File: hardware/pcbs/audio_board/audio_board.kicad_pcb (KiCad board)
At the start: 4 copper layers, 152 x 117.3 mm, 150 parts, among them J1 I2C, J10 Stereo Line-in, J2 Conn_01x08, J3 NC3MAH, J4 AudioJack3, J5 NC3MAH, J6 NC3FAH1, J7 NC3FAH1, J8 NC3FAH1, J9 DECT, Q1 S8050, Q2 2N7002, Q3 SI2309CDS-T1-GE3, Q4 2N7002, Q5 SI2309CDS-T1-GE3, Q6 2N7002, Q7 SI2309CDS-T1-GE3, U2 LP5907MFX-3.3, U3 LM5158, U4 TAD5242, U5 TAD5242, U6 TAA3040

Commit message: route some more
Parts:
- added C9: 0.1uF, Capacitor_SMD:C_0805_2012Metric, F.Cu at (88.5, 99.8)
- added R54: 510, Resistor_SMD:R_0805_2012Metric, F.Cu at (191.0, 92.5)
- C4: value 22uF -> 47uF; footprint Capacitor_SMD:C_0805_2012Metric -> Capacitor_THT:CP_Radial_D5.0mm_P2.00mm
- moved J1 129.0 mm to (89.5, 91.5)
- moved C1 120.8 mm to (85.0, 126.1), turned to 180 degrees
- moved D2 119.6 mm to (85.8, 118.8), turned to 180 degrees
- moved L1 119.4 mm to (73.2, 118.8), turned to 0 degrees
- moved Q1 119.2 mm to (75.8, 122.0)
- moved U2 119.0 mm to (86.0, 122.4), turned to 90 degrees
- moved R10 118.8 mm to (72.8, 122.0)
- moved C3 118.8 mm to (89.0, 122.0)
- moved C33 118.5 mm to (173.8, 111.8)
- moved C34 117.3 mm to (173.8, 108.0)
- moved C29 117.0 mm to (161.8, 107.0), turned to 135 degrees
- moved R6 116.1 mm to (127.5, 94.5)
- moved D1 116.1 mm to (80.2, 125.8)
- moved C28 115.8 mm to (163.5, 110.8), turned to 135 degrees
- moved C4 115.6 mm to (80.8, 122.0)
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- renumbered C9 to C10, C10 to C11, C11 to C12, C12 to C13, C13 to C14, C14 to C15, C15 to C16, C16 to C17, C17 to C18, C18 to C19, C19 to C20, C20 to C21, C21 to C22, C22 to C23, C23 to C24, C24 to C25, C25 to C26, C26 to C27, C27 to C28, C28 to C29, C29 to C30, C30 to C31, C31 to C32, C32 to C33, C33 to C34, C34 to C35, C35 to C36, C36 to C37, C37 to C38, C38 to C39, C39 to C40, C40 to C41, C41 to C42, C42 to C43, C43 to C44, C44 to C45, C45 to C46, C46 to C47, C47 to C48, C48 to C49, C49 to C50, C50 to C51, C51 to C52, C52 to C53, C53 to C54, R54 to R55, R55 to R56
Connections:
- C41 pad 2: /ADC/IN1+ -> /ADC/IN2+
- C42 pad 2: /ADC/IN1- -> /ADC/IN2-
- C47 pad 2: /ADC/IN2+ -> /ADC/IN1+
- C48 pad 2: /ADC/IN2- -> /ADC/IN1-
- D4 pad 2: /ADC/IN1+ -> /ADC/IN2+
- D4 pad 3: /ADC/IN1- -> /ADC/IN2-
- D5 pad 2: /ADC/IN2+ -> /ADC/IN1+
- D5 pad 3: /ADC/IN2- -> /ADC/IN1-
- J10 pad S: GND -> /ADC/IN4-
- Q2 pad 1: /PHANTOM_IN1_EN -> /PHANTOM_IN2_EN
- Q4 pad 1: /PHANTOM_IN2_EN -> /PHANTOM_IN1_EN
- R18 pad 1: /PHANTOM_IN1_EN -> /PHANTOM_IN2_EN
- R28 pad 1: /ADC/IN1+ -> /ADC/IN2+
- R29 pad 2: /ADC/IN1- -> /ADC/IN2-
- R30 pad 1: /PHANTOM_IN2_EN -> /PHANTOM_IN1_EN
- R40 pad 1: /ADC/IN2+ -> /ADC/IN1+
- R41 pad 2: /ADC/IN2- -> /ADC/IN1-
- U6 pad 13: GND -> /ADC/IN4-
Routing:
- net +48V: track 8.09 -> 212.0 mm
- net +3.3VA: track 22.6 -> 197.3 mm, vias 3 -> 8
- net GND: track 18.0 -> 135.4 mm, vias 24 -> 32
- net /ADC/IN1+: track 8.14 -> 46.8 mm
- net /ADC/IN1-: track 8.08 -> 44.5 mm
- net /ADC/IN4-: track 0.00 -> 36.3 mm
- net +5V: track 36.7 -> 67.9 mm
- net /ADC/IN3-: track 8.08 -> 33.9 mm
- net /ADC/IN3+: track 8.14 -> 30.1 mm
- net +5VA: track 0.00 -> 19.3 mm
- net Net-(J10-PadT): track 0.00 -> 14.0 mm
- net /ADC/IN4+: track 0.00 -> 13.7 mm
- net +3.3V: track 19.1 -> 32.2 mm, vias 0 -> 2
- net Net-(J10-PadR): track 0.00 -> 11.5 mm
- net Net-(D1-K): track 0.00 -> 11.0 mm
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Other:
- board size 152 x 117.3 mm -> 152 x 61.5 mm

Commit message: routing almost complete
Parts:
- added C5: 1μF, Capacitor_SMD:C_0805_2012Metric, F.Cu at (175.0, 123.0)
- added C6: 1μF, Capacitor_SMD:C_0805_2012Metric, F.Cu at (119.0, 128.0)
- J9: value DECT -> Conn_01x12; footprint extra:DectModule -> Connector_PinHeader_2.54mm:PinHeader_1x12_P2.54mm_Vertical
- moved J9 94.9 mm to (99.5, 109.5), turned to 90 degrees
- moved J1 31.2 mm to (109.4, 115.5), turned to 90 degrees
- moved J10 22.8 mm to (206.8, 98.2)
- moved R54 11.5 mm to (200.2, 99.2), turned to 90 degrees
- moved J2 1.38 mm to (178.6, 97.8)
- moved R6 0.75 mm to (127.5, 93.8), turned to -90 degrees
- moved Q4 0.75 mm to (127.1, 135.4)
- moved R32 0.40 mm to (128.7, 132.5)
- moved R30 0.29 mm to (124.2, 135.2)
- moved U1 0.16 mm to (102.0, 98.2)
- turned R1 to -90 degrees
- turned R2 to -90 degrees
- turned R3 to -90 degrees
- turned R4 to -90 degrees
- renumbered C8 to C10, C9 to C11, C10 to C12, C11 to C13, C12 to C14, C13 to C15, C14 to C16, C15 to C17, C16 to C18, C17 to C19, C18 to C20, C19 to C21, C20 to C22, C21 to C23, C22 to C24, C23 to C25, C24 to C26, C25 to C27, C26 to C28, C27 to C29, C28 to C30, C29 to C31, C30 to C32, C31 to C33, C32 to C34, C33 to C35, C34 to C36, C35 to C37, C36 to C38, C37 to C39, C38 to C40, C39 to C41, C40 to C42, C41 to C43, C42 to C44, C43 to C45, C44 to C46, C45 to C47, C46 to C48, C47 to C49, C48 to C50, C49 to C51, C50 to C52, C51 to C53, C52 to C54, C53 to C55, C54 to C56, C5 to C7, C6 to C8, C7 to C9
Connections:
- J9 pad 10: /DECT_INT -> /DECT_RX
- J9 pad 11: /SCL -> /DECT_TX
- J9 pad 12: /SDA -> GND
- J9 pad 2: /I2S2_RX -> /I2S2_TX
- J9 pad 3: /I2S2_TX -> /I2S2_FS
- J9 pad 4: /I2S2_FS -> /I2S2_BCLK
- J9 pad 5: /I2S2_BCLK -> /I2S2_RX
- J9 pad 6: GND -> /SCL
- J9 pad 7: /DECT_RX -> /SDA
- J9 pad 8: /DECT_TX -> /DECT_INT
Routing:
- net +3.3V: track 32.2 -> 289.2 mm, vias 2 -> 4
- net /I2S1_LRCLK: track 15.9 -> 194.9 mm, vias 1 -> 5
- net /I2S1_BCLK: track 17.8 -> 183.7 mm, vias 1 -> 5
- net /DAC 1/DOUT: track 6.03 -> 153.7 mm, vias 0 -> 2
- net GND: track 135.4 -> 214.3 mm, vias 32 -> 56
- net /SDA1: track 7.99 -> 79.1 mm, vias 1 -> 2
- net /SCL1: track 9.59 -> 76.0 mm, vias 1 -> 2
- net /CS_RIGHT: track 0.00 -> 61.3 mm, vias 0 -> 2
- net /CS_LEFT: track 0.00 -> 60.9 mm, vias 0 -> 2
- net Net-(J2-Pin_7): track 0.00 -> 59.2 mm
- net /I2S1_RX1: track 7.66 -> 65.7 mm
- net Net-(J2-Pin_6): track 0.00 -> 48.5 mm
- net /DC: track 0.00 -> 43.8 mm
- net /RESET: track 0.00 -> 34.9 mm
- net /I2S1_TX1: track 2.37 -> 37.1 mm, vias 0 -> 1
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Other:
- board text removed: "5V"
- board text removed: "DECT Module"
- board text removed: "GND"
- board text removed: "Headphones (OUT3/4)"
- board text removed: "INT"
- board text removed: "RESET"
- board text removed: "SCL"
- board text removed: "SDA"
- board text removed: "TDM BCLK"
- board text removed: "TDM FS"
- board text removed: "TDM RX"
- board text removed: "TDM TX"
- board text removed: "UART RX"
- board text removed: "UART TX"
- board text removed: "USB"

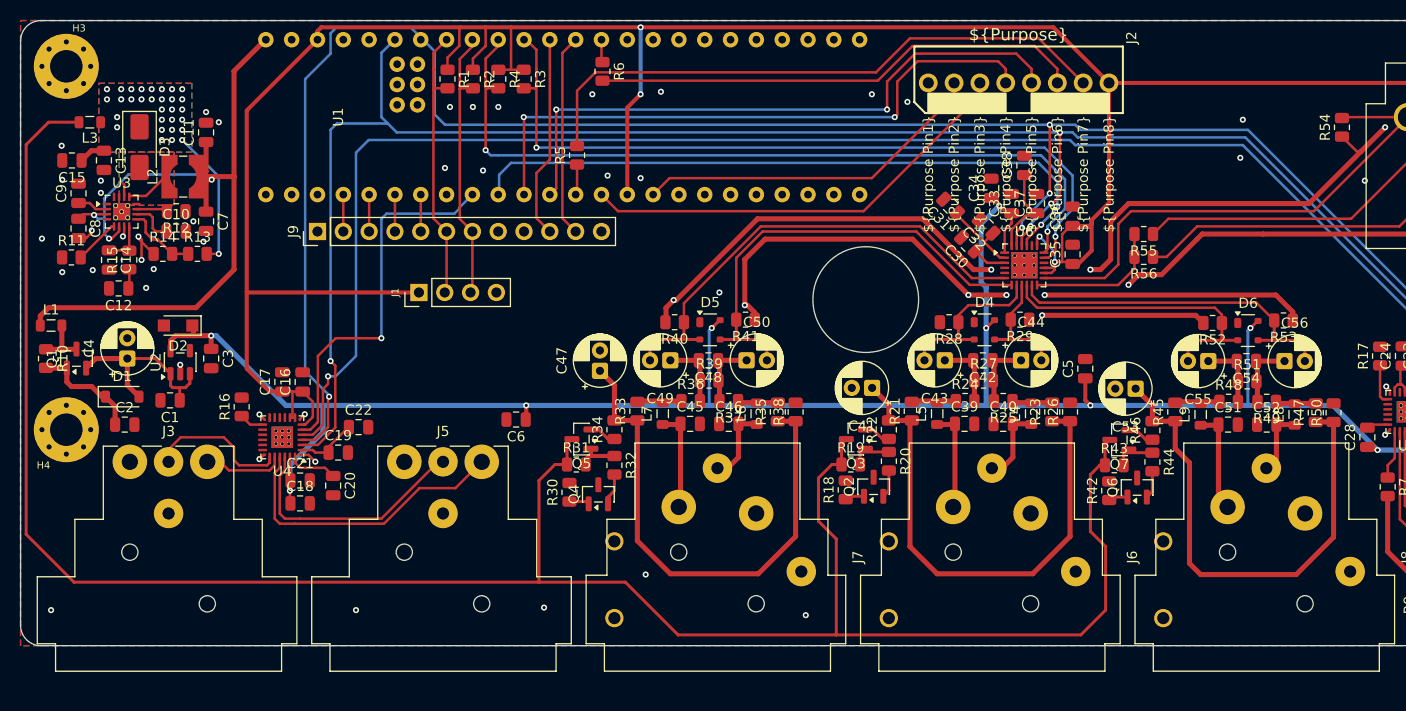
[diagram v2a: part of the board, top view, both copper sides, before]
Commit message: fix XLR courtyard
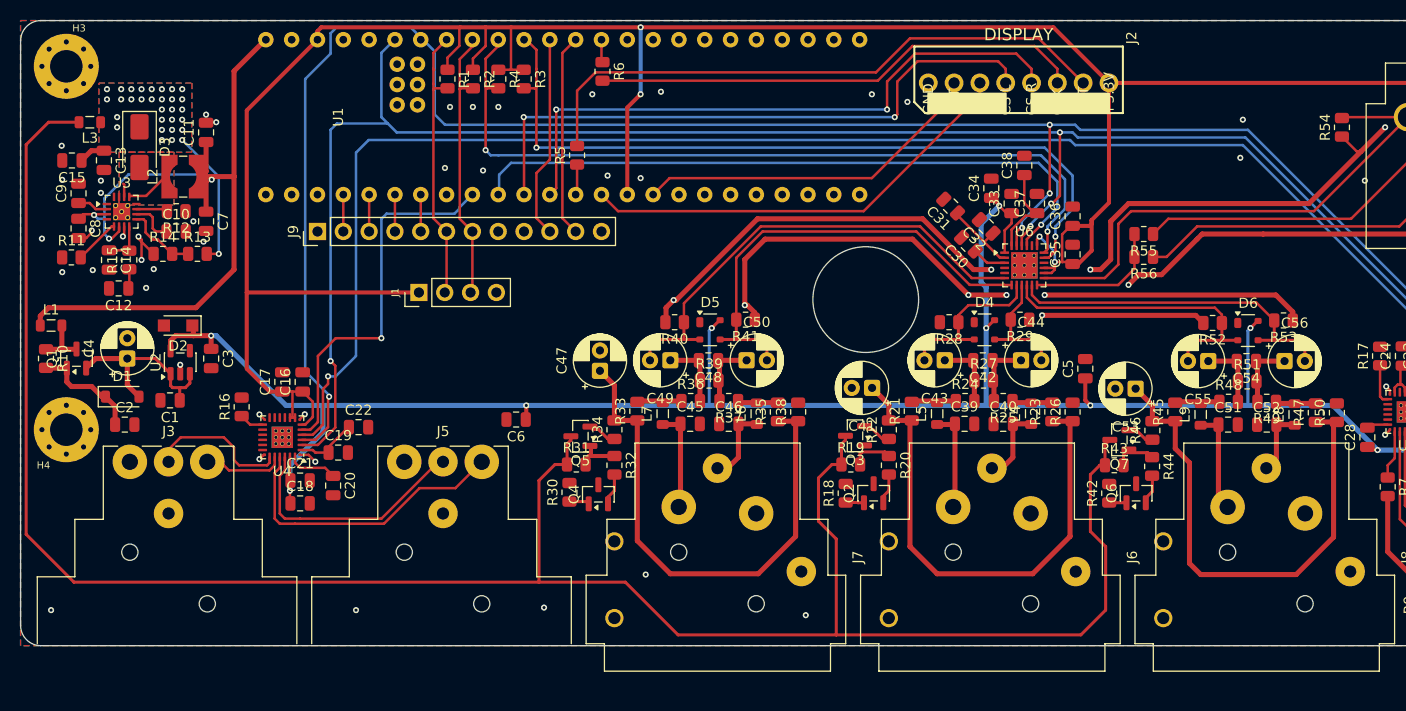
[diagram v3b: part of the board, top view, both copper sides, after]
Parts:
- J2: value Conn_01x08 -> MTA100_08
- moved Q2 0.64 mm to (154.2, 135.2)
- moved Q6 0.57 mm to (180.0, 135.2)
- moved R44 0.44 mm to (181.6, 132.6)
- moved R20 0.40 mm to (155.7, 132.5)
- moved Q3 0.34 mm to (152.3, 129.6)
- moved R18 0.32 mm to (151.4, 135.2)
- moved R50 0.32 mm to (199.8, 127.3)
- moved Q5 0.30 mm to (125.3, 129.6)
- moved R26 0.25 mm to (173.8, 127.2)
- moved R38 0.25 mm to (146.8, 127.2)
- moved R42 0.25 mm to (177.3, 135.2)
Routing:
- net +48V: track 212.0 -> 212.5 mm
- net GND: vias 56 -> 58
- net (no net): vias 3 -> 0

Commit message: connect some items
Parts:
- moved Q6 0.38 mm to (180.0, 135.6)
- moved Q7 0.16 mm to (178.3, 129.8)
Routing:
- net /PHANTOM_IN3_EN: track 2.42 -> 89.6 mm, vias 0 -> 7
- net /PHANTOM_IN1_EN: track 2.11 -> 58.2 mm, vias 0 -> 3
- net /DECT_INT: track 0.00 -> 51.1 mm, vias 0 -> 2
- net /PHANTOM_IN2_EN: track 1.81 -> 50.4 mm, vias 0 -> 5
- net /DECT_RESET: track 0.00 -> 48.2 mm, vias 0 -> 2
- net Net-(J4-PadS): track 18.7 -> 37.8 mm
- net +5V: track 79.3 -> 87.5 mm, vias 3 -> 5
- net GND: track 214.3 -> 221.2 mm, vias 58 -> 64
- net +3.3V: track 289.2 -> 293.4 mm
- net /DC: track 43.8 -> 42.5 mm, vias 0 -> 1
- net Net-(C41-Pad1): track 50.7 -> 49.9 mm
- net /I2S1_BCLK: track 183.7 -> 184.3 mm
- net /I2S1_LRCLK: track 194.9 -> 195.4 mm
- net /RESET: vias 0 -> 1

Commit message: finish routing
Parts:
- removed the R8 at (207.8, 134.6)
- renumbered R11 to R10, R12 to R11, R13 to R12, R14 to R13, R15 to R14, R16 to R15, R17 to R16, R18 to R17, R19 to R18, R20 to R19, R21 to R20, R22 to R21, R23 to R22, R24 to R23, R25 to R24, R26 to R25, R27 to R26, R28 to R27, R29 to R28, R30 to R29, R31 to R30, R32 to R31, R33 to R32, R34 to R33, R35 to R34, R36 to R35, R37 to R36, R38 to R37, R39 to R38, R40 to R39, R41 to R40, R42 to R41, R43 to R42, R44 to R43, R45 to R44, R46 to R45, R47 to R46, R48 to R47, R49 to R48, R50 to R49, R51 to R50, R52 to R51, R53 to R52, R54 to R53, R55 to R54, R56 to R55, R9 to R8, R10 to R9
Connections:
- J4 pad S: Net-(J4-PadS) -> /HP_GND
- R7 pad 2: Net-(J4-PadS) -> /HP_GND
- R8 pad 2: Net-(J4-PadS) -> /HP_GND
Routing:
- net /HP_GND: track 4.85 -> 43.7 mm
- net Net-(J4-PadS): track 37.8 -> 0.00 mm
- net GND: track 221.2 -> 246.9 mm, vias 64 -> 252
- net /I2S1_LRCLK: track 195.4 -> 194.4 mm
- net Net-(Q3-G): track 4.12 -> 4.77 mm
